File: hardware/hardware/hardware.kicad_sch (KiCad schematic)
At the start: 41 parts, among them M1 Stepper_Motor_unipolar_5pin, M2 Stepper_Motor_unipolar_5pin, M3 Stepper_Motor_unipolar_5pin, SW1 SW_Push_SPDT, SW10 SW_Push_SPDT, SW11 SW_Push_SPDT, SW12 SW_Push_SPDT, SW13 SW_Push_SPDT, SW14 SW_Push_SPDT, SW15 SW_Push_SPDT, SW16 SW_Push_SPDT, SW17 SW_Push, SW2 SW_Push_SPDT, SW3 SW_Push_SPDT, SW4 SW_Push_SPDT, SW5 SW_Push_SPDT, SW6 SW_Push_SPDT, SW7 SW_Push_SPDT, SW8 SW_Push_SPDT, SW9 SW_Push_SPDT, U1 WeMos_D1_mini, U2 CD4051B, U3 CD4051B, U4 ULN2003A, U5 ULN2003A, U6 ULN2003A

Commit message: Added latest schematic and pcb design
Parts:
- added R13, R14, R15, R16, R17, R18, R19: 1K, symbol Device:R
- added R20: 10K, symbol Device:R
- M1, M2, M3: footprint (none) -> Connector_JST:JST_XH_B5B-XH-A_1x05_P2.50mm_Vertical; Connector (none) -> https://www.conrad.at/de/p/jst-stiftleiste-standard-xh-polz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
- R12: value 10K -> 1K
- SW1, SW10, SW11, SW12, SW13, SW14, SW15, SW16, SW2, SW3, SW4, SW5, SW6, SW7, SW8, SW9: footprint (none) -> MS0850502F030P1A:SW_MS0850502F030P1A
- U2, U3: footprint (none) -> Package_SO:SOIC-16_3.9x9.9mm_P1.27mm; LCSC PN (none) -> C21379
- U4, U5, U6: footprint (none) -> Package_SO:SOIC-16_3.9x9.9mm_P1.27mm; LCSC PN (none) -> C7512
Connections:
- net +5V: now also R3.1; no longer R2.1
- net B: now also R3.2; no longer R2.2
- net GND: now also R12.1, R2.1, R13.1, R14.1, R15.1, R16.1, R17.1, R18.1, R19.1, R20.2; no longer R12.2, R3.1
- net IN3: now also R2.2; no longer R3.2
- net SW1: now also R20.1; no longer R12.1
- net SW10: now also SW10.2 (B), R13.2
- net SW11: now also SW11.2 (B), R14.2
- net SW12: now also SW12.2 (B), R15.2
- net SW13: now also SW13.2 (B), R16.2
- net SW14: now also SW14.2 (B), R17.2
- net SW15: now also SW15.2 (B), R18.2
- net SW16: now also SW16.2 (B), R19.2
- net SW9: now also R12.2, SW9.2 (B)

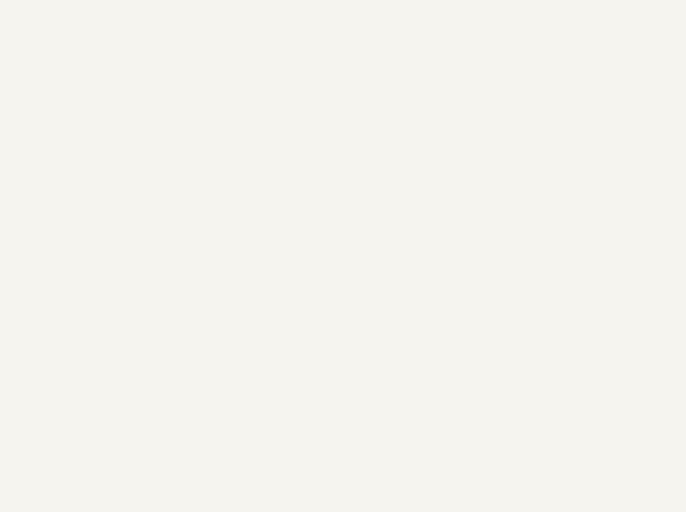
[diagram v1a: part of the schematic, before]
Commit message: added continuous rotation to stepper
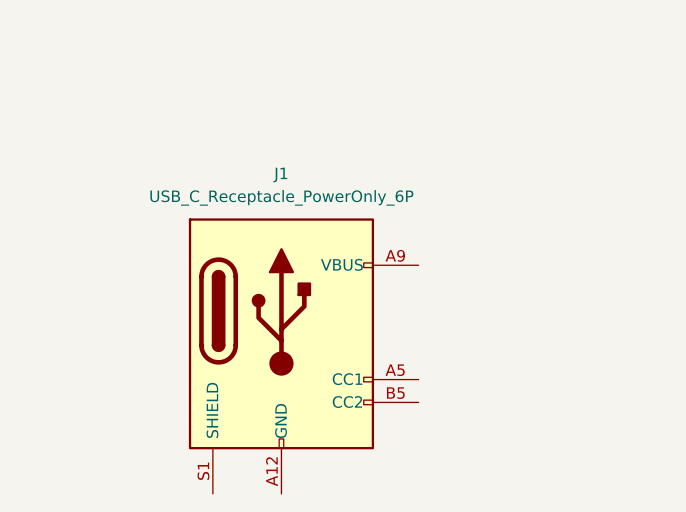
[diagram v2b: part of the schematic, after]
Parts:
- added J1: USB_C_Receptacle_PowerOnly_6P, Connector_USB:USB_C_Receptacle_GCT_USB4125-xx-x-0190_6P_TopMnt_Horizontal, symbol Connector:USB_C_Receptacle_PowerOnly_6P
- M1: footprint Connector_JST:JST_XH_B5B-XH-A_1x05_P2.50mm_Vertical -> Connector_JST:JST_XH_S5B-XH-A-1_1x05_P2.50mm_Horizontal
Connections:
- new net: J1.A12 (GND), J1.B12 (GND)
- new net: J1.A9 (VBUS), J1.B9 (VBUS)
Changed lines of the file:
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@@
 			)
 		)
-		(property "Footprint" "Connector_JST:JST_XH_B5B-XH-A_1x05_P2.50mm_Vertical"
+		(property "Footprint" "Connector_JST:JST_XH_S5B-XH-A-1_1x05_P2.50mm_Horizontal"
 			(at 205.994 139.446 0)
 			(effects
@@
 					(unit 1)
 				)
+			)
+		)
+	)
+	(symbol
+		(lib_id "Connector:USB_C_Receptacle_PowerOnly_6P")
+		(at 43.18 168.91 0)
+		(unit 1)
+		(exclude_from_sim no)
+		(in_bom yes)
+		(on_board yes)
+		(dnp no)
+		(fields_autoplaced yes)
+		(property "Reference" "J1"
+			(at 43.18 151.13 0)
+			(effects
+				(font
+					(size 1.27 1.27)
+				)
+			)
+		)
+		(property "Value" "USB_C_Receptacle_PowerOnly_6P"
+			(at 43.18 153.67 0)
+			(effects
+				(font
+					(size 1.27 1.27)
+				)
+			)
+		)
+		(property "Footprint" "Connector_USB:USB_C_Receptacle_GCT_USB4125-xx-x-0190_6P_TopMnt_Horizontal"
+			(at 46.99 166.37 0)
+			(effects
+				(font
+					(size 1.27 1.27)
+				)
+				(hide yes)
+			)
+		)
+		(property "Datasheet" "https://www.usb.org/sites/default/files/documents/usb_type-c.zip"
+			(at 43.18 168.91 0)
+			(effects
+				(font
+					(size 1.27 1.27)
+				)
+				(hide yes)
+			)
+		)
+		(property "Description" "USB Power-Only 6P Type-C Receptacle connector"
+			(at 43.18 168.91 0)
+			(effects
+				(font
+					(size 1.27 1.27)
+				)
+				(hide yes)
+			)
+		)
+		(pin "B5"
+		)
+		(pin "B12"
+		)
+		(pin "A5"
+		)
+		(pin "A12"
+		)
+		(pin "S1"
+		)
+		(pin "B9"
+		)
+		(pin "A9"
+		)
+		(instances
+			(project ""
+				(path "/a919565d-80d2-4c4e-90a0-c07f5d8b00ec"
+					(reference "J1")
+					(unit 1)
+				)

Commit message: added final pcb design
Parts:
- removed J1: USB_C_Receptacle_PowerOnly_6P, Connector_USB:USB_C_Receptacle_GCT_USB4125-xx-x-0190_6P_TopMnt_Horizontal, symbol Connector:USB_C_Receptacle_PowerOnly_6P
- removed SW17: SW_Push, symbol Switch:SW_Push
- added C10, C11, C12, C13, C14, C4, C5, C6, C7, C8, C9: 10pF, Capacitor_SMD:C_0805_2012Metric, symbol Device:C
- added J2: Barrel_Jack, Connector_BarrelJack:BarrelJack_CUI_PJ-063AH_Horizontal, symbol Connector:Barrel_Jack
- added M10, M11, M12, M13, M14, M4, M5, M6, M7, M8, M9: Stepper_Motor_unipolar_5pin, Connector_Audio:HOOYA-PJ-3505A_C19190915-Jack_3.5mm_PJ31060-I_Horizontal, symbol Motor:Stepper_Motor_unipolar_5pin
- added U10, U11, U12, U13, U14, U15, U16, U17, U7, U8, U9: ULN2003A, Package_SO:SOIC-16_3.9x9.9mm_P1.27mm, symbol Transistor_Array:ULN2003A
- C1, C2, C3: footprint (none) -> Capacitor_SMD:C_0805_2012Metric; LCSC PN (none) -> C157608
- M1: footprint Connector_JST:JST_XH_S5B-XH-A-1_1x05_P2.50mm_Horizontal -> Connector_Audio:HOOYA-PJ-3505A_C19190915-Jack_3.5mm_PJ31060-I_Horizontal; LCSC PN (none) -> C19190915
- M2, M3: footprint Connector_JST:JST_XH_B5B-XH-A_1x05_P2.50mm_Vertical -> Connector_Audio:HOOYA-PJ-3505A_C19190915-Jack_3.5mm_PJ31060-I_Horizontal; LCSC PN (none) -> C19190915
- R1, R10, R11, R12, R13, R14, R15, R16, R17, R18, R19, R2, R3, R4, R5, R6, R7, R8, R9: footprint (none) -> Resistor_SMD:R_0805_2012Metric; LCSC PN (none) -> C25623
- R20: footprint (none) -> Resistor_SMD:R_0805_2012Metric; LCSC PN (none) -> C2930231
- U1: now not fitted
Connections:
- net +5V: now also C10.1, C11.1, C12.1, C13.1, C14.1, C4.1, C5.1, C6.1, C7.1, C8.1, C9.1, J2.1, M10.1, M11.1, M12.1, M13.1, M14.1, M4.1, M5.1, M6.1, M7.1, M8.1, M9.1, U10.9 (COM), U11.9 (COM), U12.9 (COM), U13.9 (COM), U14.9 (COM), U15.9 (COM), U16.9 (COM), U17.9 (COM), U7.9 (COM), U8.9 (COM), U9.9 (COM)
- net BLUE1: now also M5.5, M9.5, U12.16 (O1), U8.16 (O1)
- net BLUE2: now also M10.5, M6.5, U13.16 (O1), U9.16 (O1)
- net BLUE3: now also M11.5, M12.5, M13.5, M14.5, M4.5, M7.5, M8.5, U10.16 (O1), U11.16 (O1), U14.16 (O1), U15.16 (O1), U16.16 (O1), U17.16 (O1), U7.16 (O1)
- net GND: now also C10.2, C11.2, C12.2, C13.2, C14.2, C4.2, C5.2, C6.2, C7.2, C8.2, C9.2, J2.2, U10.8 (GND), U11.8 (GND), U12.8 (GND), U13.8 (GND), U14.8 (GND), U15.8 (GND), U16.8 (GND), U17.8 (GND), U7.8 (GND), U8.8 (GND), U9.8 (GND); no longer R20.2
- net IN1: now also U10.1 (I1), U11.1 (I1), U12.1 (I1), U13.1 (I1), U14.1 (I1), U15.1 (I1), U16.1 (I1), U17.1 (I1), U7.1 (I1), U8.1 (I1), U9.1 (I1)
- net IN2: now also U10.2 (I2), U11.2 (I2), U12.2 (I2), U13.2 (I2), U14.2 (I2), U15.2 (I2), U16.2 (I2), U17.2 (I2), U7.2 (I2), U8.2 (I2), U9.2 (I2)
- net IN3: now also U10.3 (I3), U11.3 (I3), U12.3 (I3), U13.3 (I3), U14.3 (I3), U15.3 (I3), U16.3 (I3), U17.3 (I3), U7.3 (I3), U8.3 (I3), U9.3 (I3)
- net IN4: now also U10.4 (I4), U11.4 (I4), U12.4 (I4), U13.4 (I4), U14.4 (I4), U15.4 (I4), U16.4 (I4), U17.4 (I4), U7.4 (I4), U8.4 (I4), U9.4 (I4)
- net ORANGE1: now also M5.2, M9.2, U12.13 (O4), U8.13 (O4)
- net ORANGE2: now also M10.2, M6.2, U13.13 (O4), U9.13 (O4)
- net ORANGE3: now also M11.2, M12.2, M13.2, M14.2, M4.2, M7.2, M8.2, U10.13 (O4), U11.13 (O4), U14.13 (O4), U15.13 (O4), U16.13 (O4), U17.13 (O4), U7.13 (O4)
- net PINK1: now also M5.3 (-), M9.3 (-), U12.15 (O2), U8.15 (O2)
- net PINK2: now also M10.3 (-), M6.3 (-), U13.15 (O2), U9.15 (O2)
- net PINK3: now also M11.3 (-), M12.3 (-), M13.3 (-), M14.3 (-), M4.3 (-), M7.3 (-), M8.3 (-), U10.15 (O2), U11.15 (O2), U14.15 (O2), U15.15 (O2), U16.15 (O2), U17.15 (O2), U7.15 (O2)
- net SW1: no longer R20.1
- net YELLOW1: now also M5.4, M9.4, U12.14 (O3), U8.14 (O3)
- net YELLOW2: now also M10.4, M6.4, U13.14 (O3), U9.14 (O3)
- net YELLOW3: now also M11.4, M12.4, M13.4, M14.4, M4.4, M7.4, M8.4, U10.14 (O3), U11.14 (O3), U14.14 (O3), U15.14 (O3), U16.14 (O3), U17.14 (O3), U7.14 (O3)
- no-connect marks 23 -> 89
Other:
- note added: "FROM HERE THE CLOLRED PINS NEED RENAMING"
- note removed: "TODO power en ground and pulldown of switched...need to be checken with propper microswitch"
- note removed: "this is how my pushbuttons are connected"
- moved on the sheet: R20

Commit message: updated pcb design
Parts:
- removed R20: 10K, Resistor_SMD:R_0805_2012Metric, symbol Device:R
- R10, R11, R12, R13, R14, R15, R16, R17, R18, R19, R4, R5, R6, R7, R8, R9: value 1K -> 10K; LCSC PN C25623 -> C2930231
- SW1, SW10, SW11, SW12, SW13, SW14, SW15, SW16, SW2, SW3, SW4, SW5: footprint MS0850502F030P1A:SW_MS0850502F030P1A -> MS0850502F030P1A:SW_MS0850502F030P1A-fixed; now not fitted; now left out of the parts list
- SW6, SW7, SW8, SW9: footprint MS0850502F030P1A:SW_MS0850502F030P1A -> MS0850502F030P1A:SW_MS0850502F030P1A-fixed; now not fitted
- U1: now left out of the parts list
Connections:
- net BLUE1: no longer M5.5, M9.5, U12.16 (O1), U8.16 (O1)
- net BLUE2: no longer M10.5, M6.5, U13.16 (O1), U9.16 (O1)
- net BLUE3: no longer M11.5, M12.5, M13.5, M14.5, M4.5, M7.5, M8.5, U10.16 (O1), U11.16 (O1), U14.16 (O1), U15.16 (O1), U16.16 (O1), U17.16 (O1), U7.16 (O1)
- net ORANGE1: no longer M5.2, M9.2, U12.13 (O4), U8.13 (O4)
- net ORANGE2: no longer M10.2, M6.2, U13.13 (O4), U9.13 (O4)
- net ORANGE3: no longer M11.2, M12.2, M13.2, M14.2, M4.2, M7.2, M8.2, U10.13 (O4), U11.13 (O4), U14.13 (O4), U15.13 (O4), U16.13 (O4), U17.13 (O4), U7.13 (O4)
- net PINK1: no longer M5.3 (-), M9.3 (-), U12.15 (O2), U8.15 (O2)
- net PINK2: no longer M10.3 (-), M6.3 (-), U13.15 (O2), U9.15 (O2)
- net PINK3: no longer M11.3 (-), M12.3 (-), M13.3 (-), M14.3 (-), M4.3 (-), M7.3 (-), M8.3 (-), U10.15 (O2), U11.15 (O2), U14.15 (O2), U15.15 (O2), U16.15 (O2), U17.15 (O2), U7.15 (O2)
- net YELLOW1: no longer M5.4, M9.4, U12.14 (O3), U8.14 (O3)
- net YELLOW2: no longer M10.4, M6.4, U13.14 (O3), U9.14 (O3)
- net YELLOW3: no longer M11.4, M12.4, M13.4, M14.4, M4.4, M7.4, M8.4, U10.14 (O3), U11.14 (O3), U14.14 (O3), U15.14 (O3), U16.14 (O3), U17.14 (O3), U7.14 (O3)
- new net BLUE10: M10.5, U13.16 (O1)
- new net BLUE11: M11.5, U14.16 (O1)
- new net BLUE12: M12.5, U15.16 (O1)
- new net BLUE13: M13.5, U16.16 (O1)
- new net BLUE14: M14.5, U17.16 (O1)
- new net BLUE4: M4.5, U7.16 (O1)
- new net BLUE5: M5.5, U8.16 (O1)
- new net BLUE6: M6.5, U9.16 (O1)
- new net BLUE7: M7.5, U10.16 (O1)
- new net BLUE8: M8.5, U11.16 (O1)
- new net BLUE9: M9.5, U12.16 (O1)
- new net ORANGE10: M10.2, U13.13 (O4)
- new net ORANGE11: M11.2, U14.13 (O4)
- new net ORANGE12: M12.2, U15.13 (O4)
- new net ORANGE13: M13.2, U16.13 (O4)
- new net ORANGE14: M14.2, U17.13 (O4)
- new net ORANGE4: M4.2, U7.13 (O4)
- new net ORANGE5: M5.2, U8.13 (O4)
- new net ORANGE6: M6.2, U9.13 (O4)
- new net ORANGE7: M7.2, U10.13 (O4)
- new net ORANGE8: M8.2, U11.13 (O4)
- new net ORANGE9: M9.2, U12.13 (O4)
- new net PINK10: M10.3 (-), U13.15 (O2)
- new net PINK11: M11.3 (-), U14.15 (O2)
- new net PINK12: M12.3 (-), U15.15 (O2)
- new net PINK13: M13.3 (-), U16.15 (O2)
- new net PINK14: M14.3 (-), U17.15 (O2)
- new net PINK4: M4.3 (-), U7.15 (O2)
- new net PINK5: M5.3 (-), U8.15 (O2)
- new net PINK6: M6.3 (-), U9.15 (O2)
- new net PINK7: M7.3 (-), U10.15 (O2)
- new net PINK8: M8.3 (-), U11.15 (O2)
- new net PINK9: M9.3 (-), U12.15 (O2)
- new net YELLOW10: M10.4, U13.14 (O3)
- new net YELLOW11: M11.4, U14.14 (O3)
- new net YELLOW12: M12.4, U15.14 (O3)
- new net YELLOW13: M13.4, U16.14 (O3)
- new net YELLOW14: M14.4, U17.14 (O3)
- new net YELLOW4: M4.4, U7.14 (O3)
- new net YELLOW5: M5.4, U8.14 (O3)
- new net YELLOW6: M6.4, U9.14 (O3)
- new net YELLOW7: M7.4, U10.14 (O3)
- new net YELLOW8: M8.4, U11.14 (O3)
- new net YELLOW9: M9.4, U12.14 (O3)
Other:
- note removed: "FROM HERE THE CLOLRED PINS NEED RENAMING"
